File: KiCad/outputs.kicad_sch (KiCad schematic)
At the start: 32 parts, among them J1 UART, J10 LED2, J13 LED3, J14 LED4, J15 LED8, J16 LED7, J17 LED6, J18 LED5, J19 LED9, J2 VDD, J20 LED10, J21 LED11, J22 LED12, J3 GND, J6 USB_C_Receptacle_USB2.0_16P, J7 Conn_01x14, J8 JTAG, J9 LED1, U7 SN74LVC8T245, U8 SN74LVC8T245

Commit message: work
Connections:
- net GPIO.18: now reaches J7.9 (Pin_9)
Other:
- moved on the sheet: J7
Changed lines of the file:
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@@
 	(wire
 		(pts
-			(xy 189.23 127) (xy 203.2 127)
+			(xy 97.79 111.76) (xy 111.76 111.76)
 		)
 		(stroke
@@
 	(global_label "GPIO.45"
 		(shape input)
-		(at 203.2 152.4 180)
+		(at 111.76 137.16 180)
 		(fields_autoplaced yes)
 		(effects
@@
 		)
 		(property "Intersheetrefs" "${INTERSHEET_REFS}"
-			(at 192.7157 152.4 0)
+			(at 101.2757 137.16 0)
 			(hide yes)
 			(show_name no)
@@
 	(global_label "GPIO.21"
 		(shape input)
-		(at 203.2 147.32 180)
+		(at 111.76 132.08 180)
 		(fields_autoplaced yes)
 		(effects
@@
 		)
 		(property "Intersheetrefs" "${INTERSHEET_REFS}"
-			(at 192.7157 147.32 0)
+			(at 101.2757 132.08 0)
 			(hide yes)
 			(show_name no)
@@
 	(global_label "GPIO.47"
 		(shape input)
-		(at 203.2 157.48 180)
+		(at 111.76 142.24 180)
 		(fields_autoplaced yes)
 		(effects
@@
 		)
 		(property "Intersheetrefs" "${INTERSHEET_REFS}"
-			(at 192.7157 157.48 0)
+			(at 101.2757 142.24 0)
 			(hide yes)
 			(show_name no)
@@
 	(global_label "GPIO.46"
 		(shape input)
-		(at 203.2 154.94 180)
+		(at 111.76 139.7 180)
 		(fields_autoplaced yes)
 		(effects
@@
 		)
 		(property "Intersheetrefs" "${INTERSHEET_REFS}"
-			(at 192.7157 154.94 0)
+			(at 101.2757 139.7 0)
 			(hide yes)
 			(show_name no)
@@
 		)
 	)
+	(global_label "GPIO.18"
+		(shape input)
+		(at 111.76 129.54 180)
+		(fields_autoplaced yes)
+		(effects
+			(font
+				(size 1.27 1.27)
+			)
+			(justify right)
+		)
+		(property "Intersheetrefs" "${INTERSHEET_REFS}"
+			(at 101.2757 129.54 0)
+			(hide yes)
+			(show_name no)
+			(do_not_autoplace no)
+			(effects
+				(font
+					(size 1.27 1.27)
+				)
+				(justify right)
+			)
+		)
+	)
 	(global_label "DataOut2"
 		(shape input)
@@
 	(global_label "GPIO.38"
 		(shape input)
-		(at 203.2 149.86 180)
+		(at 111.76 134.62 180)
 		(fields_autoplaced yes)
 		(effects
@@
 		)
 		(property "Intersheetrefs" "${INTERSHEET_REFS}"
-			(at 192.7157 149.86 0)
+			(at 101.2757 134.62 0)
 			(hide yes)
 			(show_name no)
@@
 	(symbol
 		(lib_id "Connector_Generic:Conn_01x14")
-		(at 208.28 139.7 0)
+		(at 116.84 124.46 0)
 		(unit 1)
 		(body_style 1)
@@
 		(fields_autoplaced yes)
 		(property "Reference" "J7"
-			(at 210.82 139.6999 0)
+			(at 119.38 124.4599 0)
 			(show_name no)
 			(do_not_autoplace no)
@@
 		)
 		(property "Value" "Conn_01x14"
-			(at 210.82 142.2399 0)
+			(at 119.38 126.9999 0)
 			(show_name no)
 			(do_not_autoplace no)
@@
 		)
 		(property "Footprint" "Connector_PinHeader_2.54mm:PinHeader_1x14_P2.54mm_Vertical"
-			(at 208.28 139.7 0)
+			(at 116.84 124.46 0)
 			(hide yes)
 			(show_name no)
@@
 		)
 		(property "Datasheet" ""
-			(at 208.28 139.7 0)
+			(at 116.84 124.46 0)
 			(hide yes)
 			(show_name no)
@@
 		)
 		(property "Description" "Generic connector, single row, 01x14, script generated (kicad-library-utils/schlib/autogen/connector/)"
-			(at 208.28 139.7 0)
+			(at 116.84 124.46 0)
 			(hide yes)
 			(show_name no)
@@
 		)
 		(property "LCSC" ""
-			(at 208.28 139.7 0)
+			(at 116.84 124.46 0)
 			(hide yes)
 			(show_name no)
@@
 	(symbol
 		(lib_id "power:GND")
-		(at 189.23 127 0)
+		(at 97.79 111.76 0)
 		(unit 1)
 		(body_style 1)
@@
 		(dnp no)
 		(property "Reference" "#PWR012"
-			(at 189.23 133.35 0)
+			(at 97.79 118.11 0)
 			(hide yes)
 			(show_name no)
@@
 		)
 		(property "Value" "GND"
-			(at 189.23 130.556 0)
+			(at 97.79 115.316 0)
 			(show_name no)
 			(do_not_autoplace no)
@@
 		)
 		(property "Footprint" ""
-			(at 189.23 127 0)
+			(at 97.79 111.76 0)
 			(hide yes)
 			(show_name no)
@@
 		)
 		(property "Datasheet" ""
-			(at 189.23 127 0)
+			(at 97.79 111.76 0)
 			(hide yes)
 			(show_name no)
@@
 		)
 		(property "Description" "Power symbol creates a global label with name \"GND\" , ground"
-			(at 189.23 127 0)
+			(at 97.79 111.76 0)
 			(hide yes)
 			(show_name no)
@@
 	(symbol
 		(lib_id "power:+3.3V")
-		(at 203.2 124.46 0)
+		(at 111.76 109.22 0)
 		(unit 1)
 		(body_style 1)
@@
 		(dnp no)
 		(property "Reference" "#PWR011"
-			(at 203.2 128.27 0)
+			(at 111.76 113.03 0)
 			(hide yes)
 			(show_name no)
@@
 		)
 		(property "Value" "+3.3V"
-			(at 203.2 119.38 0)
+			(at 111.76 104.14 0)
 			(show_name no)
 			(do_not_autoplace no)
@@
 		)
 		(property "Footprint" ""
-			(at 203.2 124.46 0)
+			(at 111.76 109.22 0)
 			(hide yes)
 			(show_name no)
@@
 		)
 		(property "Datasheet" ""
-			(at 203.2 124.46 0)
+			(at 111.76 109.22 0)
 			(hide yes)
 			(show_name no)
@@
 		)
 		(property "Description" "Power symbol creates a global label with name \"+3.3V\""
-			(at 203.2 124.46 0)
+			(at 111.76 109.22 0)
 			(hide yes)
 			(show_name no)

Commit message: arrange components
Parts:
- added C22, C23, C24, C25: 100n, Capacitor_SMD:C_0805_2012Metric_Pad1.18x1.45mm_HandSolder, symbol Device:C_Small
- added D3: 1N4148WS, Diode_SMD:D_SOD-323, symbol Diode:1N4148WS
- added R13, R14: 5.1k, Resistor_SMD:R_0805_2012Metric_Pad1.20x1.40mm_HandSolder, symbol Device:R_Small
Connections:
- net +24V: now also D3.1 (K); no longer J10.1 (Pin_1), J13.1 (Pin_1), J14.1 (Pin_1), J15.1 (Pin_1), J16.1 (Pin_1), J17.1 (Pin_1), J18.1 (Pin_1), J19.1 (Pin_1), J20.1 (Pin_1), J21.1 (Pin_1), J22.1 (Pin_1), J9.1 (Pin_1)
- net +3.3V: now also C22.1, C24.1
- net +5V: now also C23.1, C25.1
- net GND: now also C22.2, C23.2, C24.2, C25.2, R13.2, R14.2
- net at J6.A4 (VBUS), J6.A9 (VBUS), J6.B4 (VBUS)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: now also D3.2 (A)
- net at J6.A5 (CC1): now also R13.1
- net at J6.B5 (CC2): now also R14.1
- new net +24V_SW: J10.1 (Pin_1), J13.1 (Pin_1), J14.1 (Pin_1), J15.1 (Pin_1), J16.1 (Pin_1), J17.1 (Pin_1), J18.1 (Pin_1), J19.1 (Pin_1), J20.1 (Pin_1), J21.1 (Pin_1), J22.1 (Pin_1), J9.1 (Pin_1)
- no-connect marks 6 -> 3
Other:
- moved on the sheet: J2, J3, J6, R35, R36, R37, R38, R39, R40, R41, R42, R43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

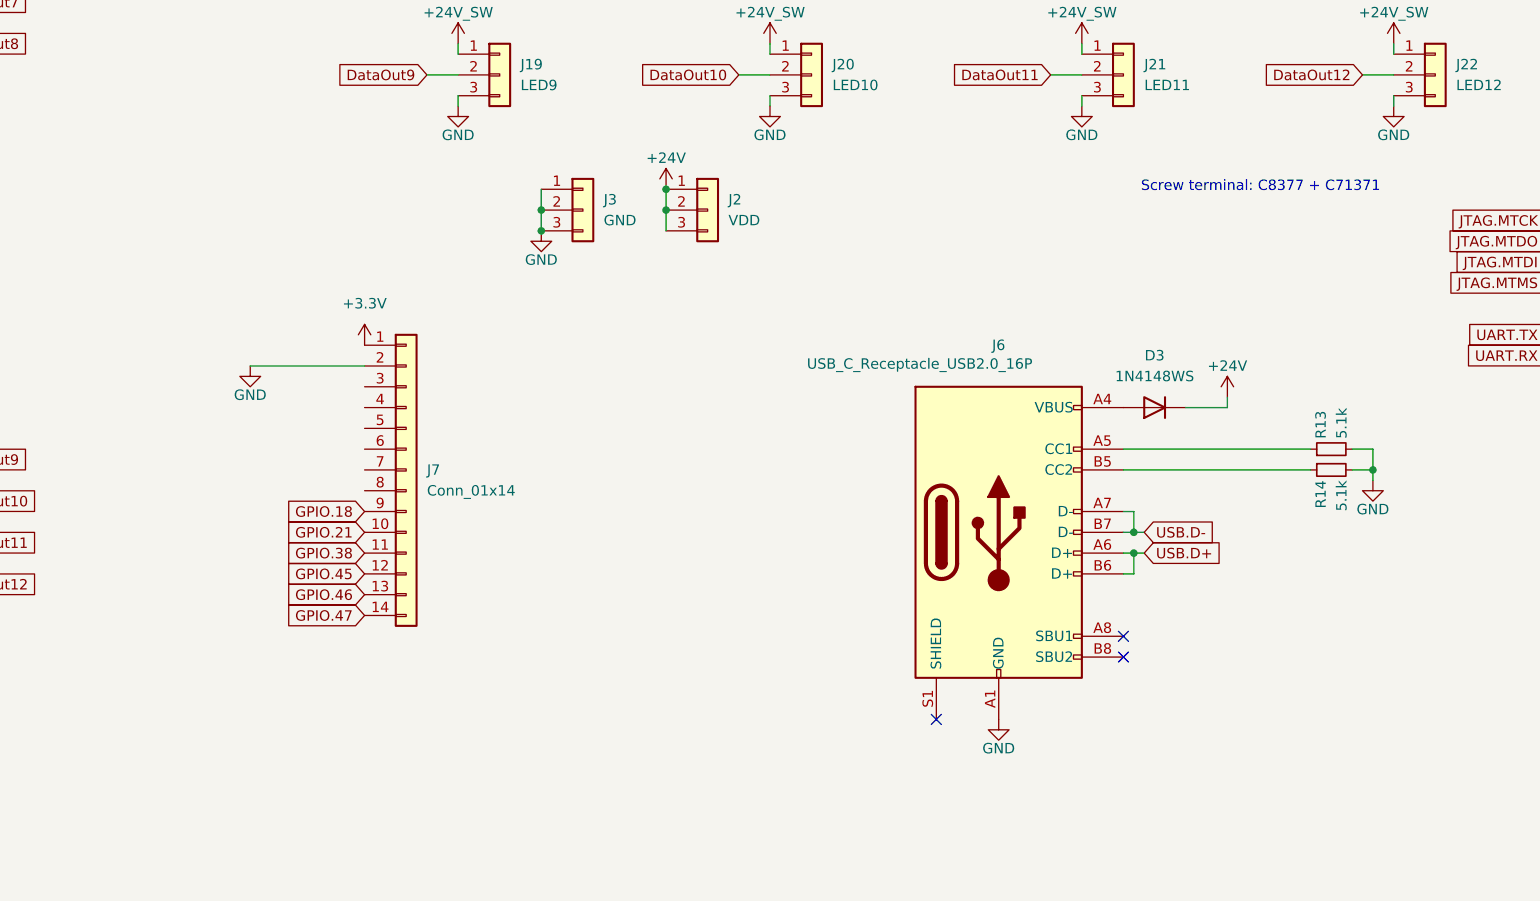
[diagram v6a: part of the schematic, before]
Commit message: init agents, change schematic
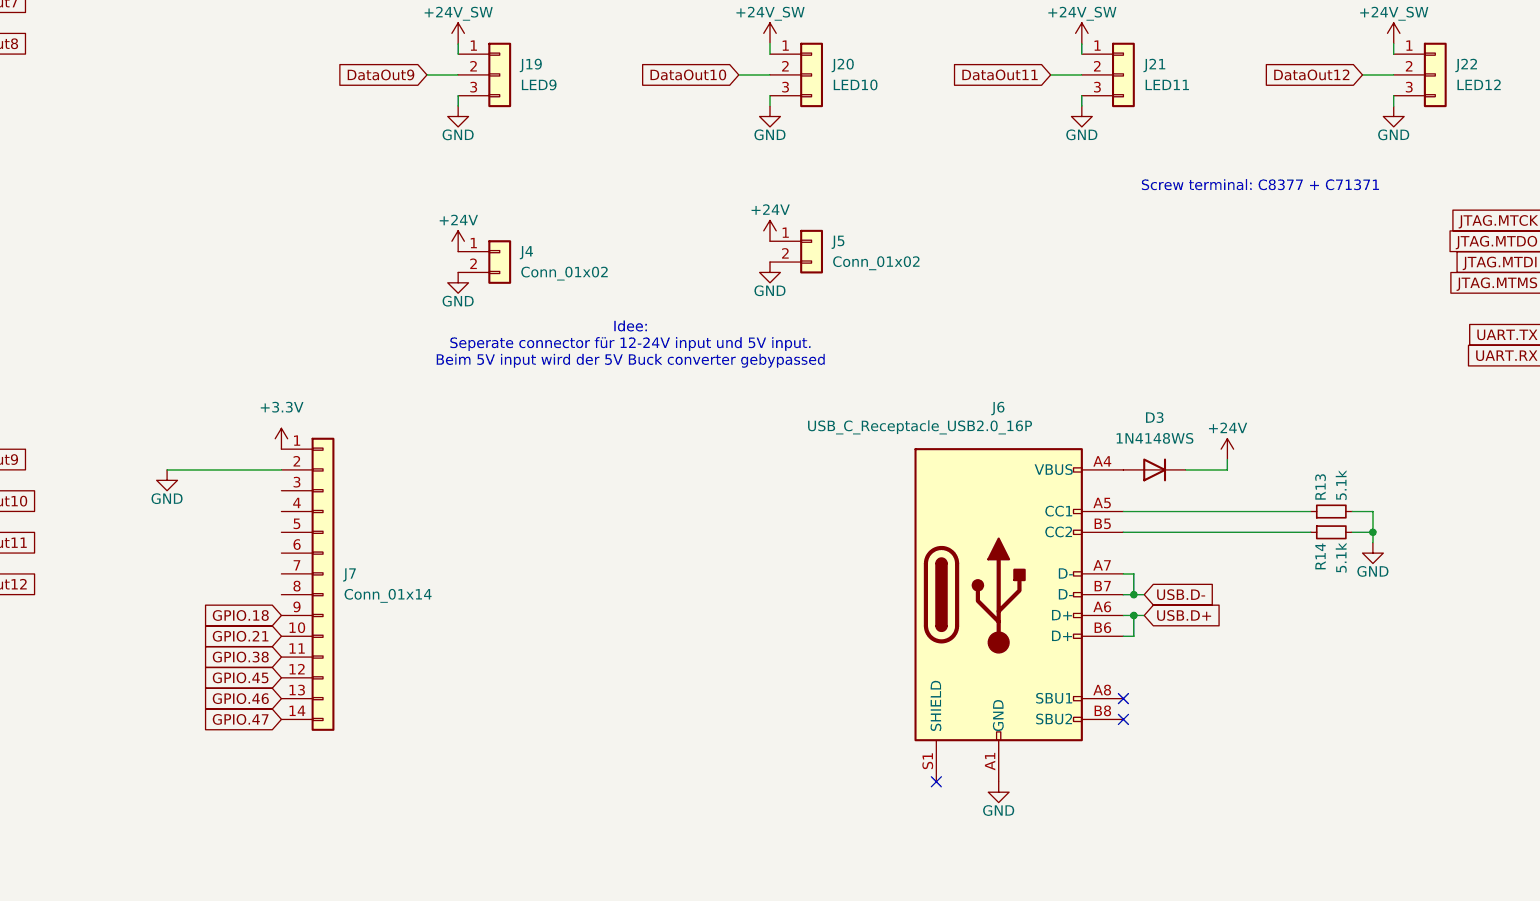
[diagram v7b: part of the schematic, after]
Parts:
- removed J2: VDD, TerminalBlock_Phoenix:TerminalBlock_Phoenix_MKDS-1,5-3-5.08_1x03_P5.08mm_Horizontal, symbol Connector_Generic:Conn_01x03
- removed J3: GND, TerminalBlock_Phoenix:TerminalBlock_Phoenix_MKDS-1,5-3-5.08_1x03_P5.08mm_Horizontal, symbol Connector_Generic:Conn_01x03
- added J4, J5: Conn_01x02, TerminalBlock_Phoenix:TerminalBlock_Phoenix_MKDS-3-2-5.08_1x02_P5.08mm_Horizontal, symbol Connector_Generic:Conn_01x02
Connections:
- net +24V: now also J4.1 (Pin_1), J5.1 (Pin_1)
- net GND: now also J4.2 (Pin_2), J5.2 (Pin_2)
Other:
- note added: "Idee: Seperate connector für 12-24V input und 5V input. Beim 5V input wird der 5V Buck converter gebypassed"
- moved on the sheet: D3, J6, J7, R13, R14
